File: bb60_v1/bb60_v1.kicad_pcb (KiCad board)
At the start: 2 copper layers, 281 x 94.4 mm, 145 parts, among them J1 Conn_01x04, SW1 SW_Push, SW2 SW_Push, U1 STM32F072CBTx, U2 XC6206PxxxMR, U3 USBLC6-2SC6

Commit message: Rerouted everything
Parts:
- moved C1 74.7 mm to (122.9, 180.2)
- moved C7 74.7 mm to (122.9, 183.8)
- moved C8 74.7 mm to (120.0, 183.8)
- moved C2 74.7 mm to (120.5, 180.2)
- moved C3 74.7 mm to (117.9, 180.2)
- moved C4 74.7 mm to (115.5, 180.2)
- moved C5 74.7 mm to (113.5, 180.2)
- moved C9 74.7 mm to (117.0, 183.8)
- moved C6 74.7 mm to (108.1, 182.0)
- moved SW1 58.4 mm to (122.6, 108.2)
- moved SW2 57.9 mm to (129.2, 108.2)
- moved R2 24.1 mm to (106.0, 86.8), turned to 0 degrees
- moved R3 22.8 mm to (106.0, 89.1), turned to 0 degrees
- moved R1 15.8 mm to (116.1, 105.2)
- moved U2 1.19 mm to (101.2, 94.5)
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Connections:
- U1 pad 10: /COL4 -> /COL7
- U1 pad 11: /COL3 -> /COL6
- U1 pad 12: /COL2 -> /COL5
- U1 pad 13: /COL1 -> /COL4
- U1 pad 16: /ROW4 -> unconnected-(U1-PA6-Pad16)
- U1 pad 17: unconnected-(U1-PA7-Pad17) -> /ROW4
- U1 pad 18: unconnected-(U1-PB0-Pad18) -> /ROW3
- U1 pad 19: /ROW0 -> /ROW2
- U1 pad 2: /COL7 -> /COL12
- U1 pad 20: unconnected-(U1-PB2-Pad20) -> /COL0
- U1 pad 21: /COL6 -> /ROW1
- U1 pad 22: /COL5 -> /ROW0
- U1 pad 29: /ROW3 -> unconnected-(U1-PA8-Pad29)
- U1 pad 3: /COL8 -> /COL11
- U1 pad 30: /ROW2 -> unconnected-(U1-PA9-Pad30)
- U1 pad 31: /COL0 -> unconnected-(U1-PA10-Pad31)
- U1 pad 37: /ROW1 -> /COL2
- U1 pad 38: unconnected-(U1-PA15-Pad38) -> /COL3
- U1 pad 4: /COL9 -> /COL10
- U1 pad 45: /COL13 -> /COL1
- U1 pad 46: /COL12 -> /COL13
- U1 pad 5: /COL10 -> /COL9
- U1 pad 6: /COL11 -> /COL8
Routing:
- net /COL13: track 82.8 -> 335.3 mm
- net /COL12: track 106.0 -> 329.2 mm
- net /ROW4: track 260.6 -> 316.5 mm, vias 0 -> 2
- net /ROW0: track 257.2 -> 285.8 mm
- net /RES_D-: track 2.77 -> 21.5 mm, vias 0 -> 2
- net +3.3V: track 0.00 -> 17.3 mm
- net /COL4: track 128.2 -> 144.7 mm, vias 1 -> 0
- net +5V: track 24.8 -> 36.6 mm
- net /RES_D+: track 4.58 -> 16.3 mm, vias 0 -> 2
- net /COL7: track 185.1 -> 195.1 mm, vias 1 -> 0
- net /COL8: track 204.4 -> 212.6 mm, vias 1 -> 0
- net GND: track 0.00 -> 8.02 mm
- net /COL9: track 223.7 -> 230.8 mm, vias 1 -> 0
- net /COL10: track 242.9 -> 248.9 mm, vias 1 -> 0
- net /COL11: track 281.9 -> 286.8 mm, vias 1 -> 0
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
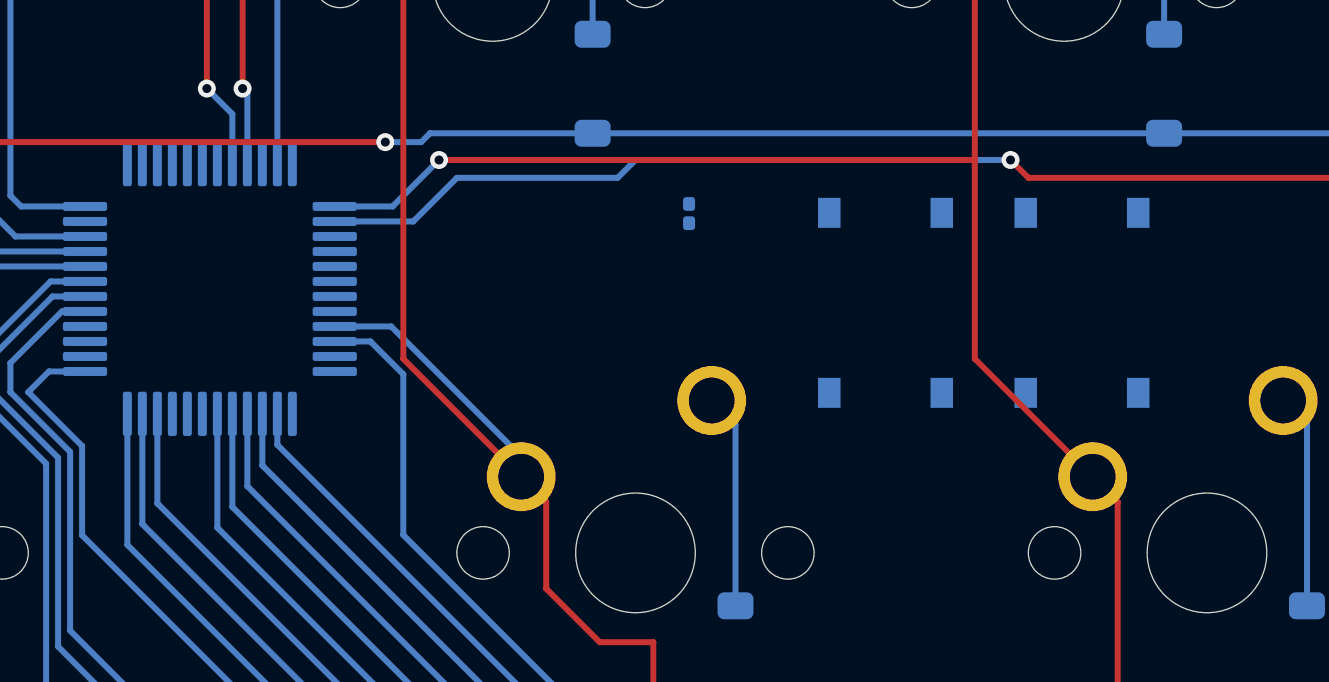
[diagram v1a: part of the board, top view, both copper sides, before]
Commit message: updated pushbuttons
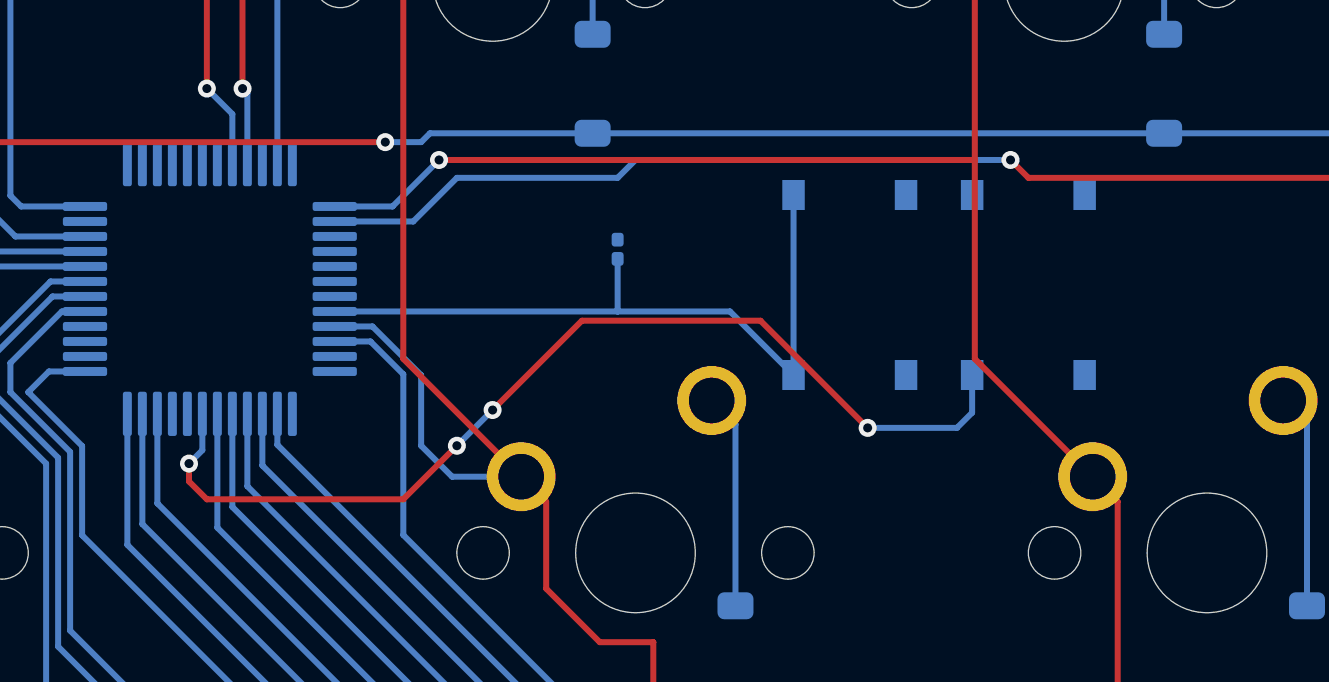
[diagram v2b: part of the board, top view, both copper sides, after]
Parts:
- moved R1 2.66 mm to (113.7, 106.4)
- moved SW2 1.88 mm to (127.4, 107.6), turned to -90 degrees
- moved SW1 1.33 mm to (121.4, 107.6), turned to -90 degrees
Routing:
- net /NRST: track 0.00 -> 34.2 mm, vias 0 -> 4
- net /BOOT0: track 0.00 -> 23.9 mm
- net /COL1: track 97.5 -> 98.5 mm

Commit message: added ground plane, completed power traces
just need bootloader and reset buttons to be routed next, also increase trace width for power cables
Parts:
- moved C7 94.4 mm to (98.2, 92.7), turned to 90 degrees
- moved C8 88.3 mm to (101.2, 97.5)
- moved C6 83.5 mm to (97.0, 99.3), turned to -90 degrees
- moved C2 81.0 mm to (93.8, 103.7), turned to -90 degrees
- moved C5 78.0 mm to (103.9, 102.8), turned to 90 degrees
- moved C3 69.9 mm to (105.4, 111.5), turned to 0 degrees
- moved C1 69.8 mm to (104.2, 113.0), turned to 0 degrees
- moved C9 69.1 mm to (101.7, 116.4), turned to 0 degrees
- moved C4 67.8 mm to (99.1, 114.4), turned to -90 degrees
- moved R1 7.98 mm to (105.8, 107.6)
- moved SW2 1.49 mm to (126.2, 106.7)
- moved SW1 1.26 mm to (120.6, 106.7)
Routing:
- net +3.3V: track 17.3 -> 54.4 mm, vias 0 -> 3
- net GND: track 8.02 -> 21.5 mm, vias 0 -> 16
- net /COL3: track 109.2 -> 112.0 mm
- net /BOOT0: track 23.9 -> 21.3 mm
- net /ROW1: track 265.9 -> 267.7 mm
- net /COL8: track 212.6 -> 211.2 mm
- net /NRST: track 34.2 -> 33.1 mm
- net /COL9: track 230.8 -> 229.7 mm
- net /COL10: track 248.9 -> 248.0 mm
- net +5V: track 36.6 -> 37.5 mm
- net /COL11: track 286.8 -> 286.3 mm
- added copper zone on B.Cu, net GND
- added copper zone on F.Cu, net GND

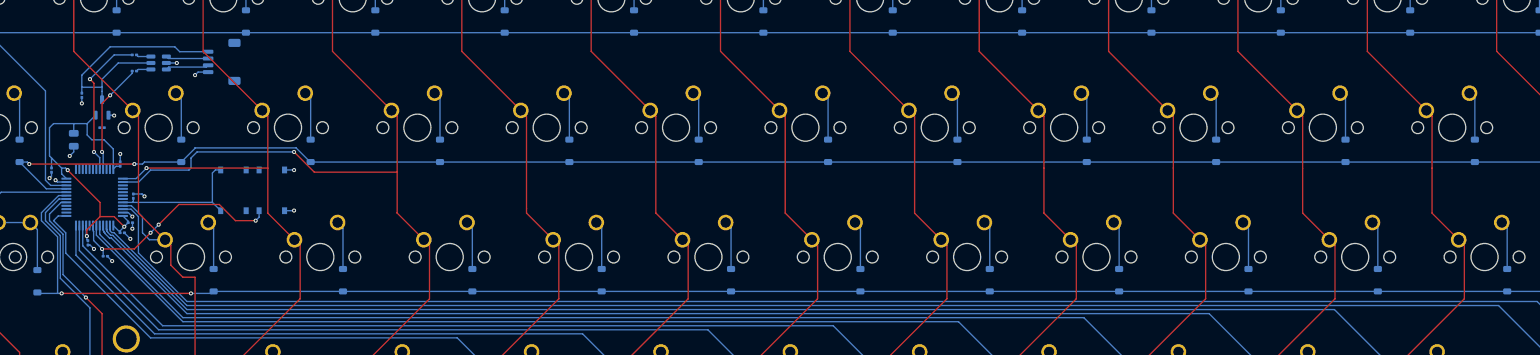
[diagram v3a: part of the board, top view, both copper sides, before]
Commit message: finished wiring everything
ratsnest gone
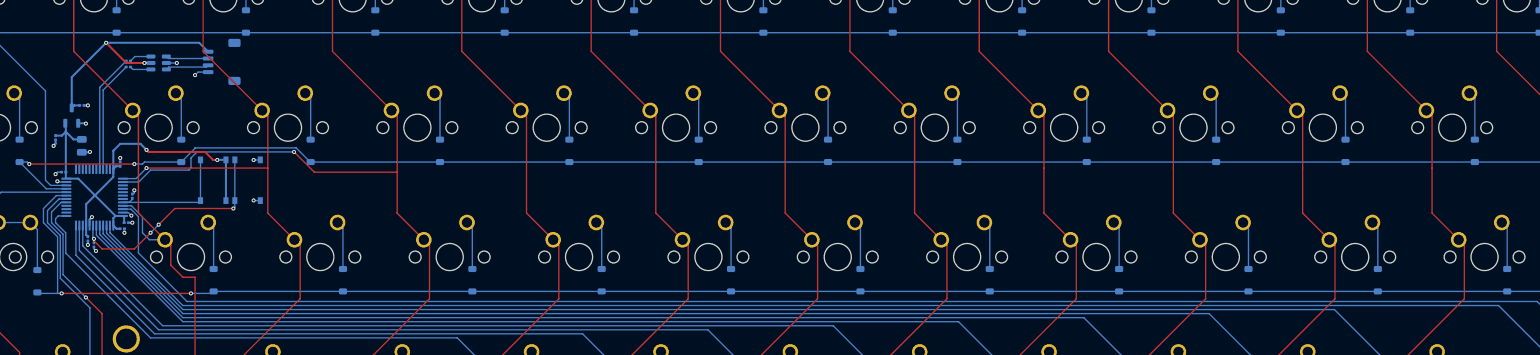
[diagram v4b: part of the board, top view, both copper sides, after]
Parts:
- moved C8 7.01 mm to (94.4, 99.0), turned to 90 degrees
- moved U2 4.62 mm to (96.7, 95.7)
- moved SW2 3.87 mm to (122.6, 105.2)
- moved SW1 3.33 mm to (117.6, 105.2)
- moved C9 2.37 mm to (100.0, 114.7), turned to -90 degrees
- moved C2 1.81 mm to (95.5, 104.0), turned to 180 degrees
- moved C7 1.49 mm to (98.2, 94.2), turned to 180 degrees
- moved C6 1.49 mm to (98.2, 100.2)
- moved R2 1.26 mm to (105.1, 87.6)
- moved R3 1.07 mm to (105.1, 88.5)
- moved C3 0.60 mm to (104.8, 111.5)
- moved C4 0.60 mm to (99.1, 113.8)
- moved C1 0.60 mm to (104.2, 112.4)
- moved R1 0.14 mm to (105.7, 107.6)
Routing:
- net +3.3V: track 54.4 -> 66.9 mm, vias 3 -> 2
- net /RES_D-: track 21.5 -> 17.5 mm, vias 2 -> 0
- net GND: track 21.5 -> 18.5 mm, vias 16 -> 18
- net /BOOT0: track 21.3 -> 19.3 mm
- net +5V: track 37.5 -> 36.4 mm, vias 0 -> 2
- net /ESD_D-: track 2.21 -> 3.28 mm
- net /ESD_D+: track 2.21 -> 3.15 mm
- net /COL11: track 286.3 -> 287.1 mm
- net /COL12: track 329.1 -> 329.8 mm
- net /NRST: track 33.1 -> 33.6 mm
- net /RES_D+: track 16.3 -> 16.4 mm, vias 2 -> 0

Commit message: Final changes
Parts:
- moved KC_RSFT1 1.43 mm to (321.5, 135.6)
- moved SW2 0.60 mm to (123.2, 105.2)
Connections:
- U1 pad 37: /COL2 -> unconnected-(U1-PA14-Pad37)
- U1 pad 38: /COL3 -> /COL2
- U1 pad 39: unconnected-(U1-PB3-Pad39) -> /COL3
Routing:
- net GND: track 18.5 -> 19.7 mm
